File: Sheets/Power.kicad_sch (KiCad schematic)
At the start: 36 parts, among them J201 JST-XH 6P, Q201 FDV301N, Q202 FDV301N, Q203 SSF3365, SW201 SW, U201 LM2678SX-5.0, U202 BQ7720700DSSR, U203 LM2675M-12

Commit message: Rev 2.1 Add pcb and footprint changes
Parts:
- J201: footprint Connector_JST:JST_XH_B6B-XH-A_1x06_P2.50mm_Vertical -> Connector_JST:JST_XH_S6B-XH-A-1_1x06_P2.50mm_Horizontal
- Q203: footprint (none) -> Package_TO_SOT_SMD:SOT-23-3
- SW201, TH201: footprint Connector_JST:JST_ZH_B2B-ZR_1x02_P1.50mm_Vertical -> Connector_JST:JST_ZH_S2B-ZR-SM4A-TF_1x02-1MP_P1.50mm_Horizontal
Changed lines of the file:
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@@
 		(title "Cyclops (Team 30)")
 		(date "2025-11-28")
-		(rev "2.0")
+		(rev "2.1")
 		(company "Concordia University, Department of Electrical and Computer Engineering")
 	)
@@
 			)
 		)
-		(property "Footprint" "Connector_JST:JST_ZH_B2B-ZR_1x02_P1.50mm_Vertical"
+		(property "Footprint" "Connector_JST:JST_ZH_S2B-ZR-SM4A-TF_1x02-1MP_P1.50mm_Horizontal"
 			(at 107.95 46.99 0)
 			(effects
@@
 			)
 		)
-		(property "Footprint" "Connector_JST:JST_XH_B6B-XH-A_1x06_P2.50mm_Vertical"
+		(property "Footprint" "Connector_JST:JST_XH_S6B-XH-A-1_1x06_P2.50mm_Horizontal"
 			(at 55.88 73.66 0)
 			(effects
@@
 			)
 		)
-		(property "Footprint" ""
+		(property "Footprint" "Package_TO_SOT_SMD:SOT-23-3"
 			(at 182.88 22.86 0)
 			(effects
@@
 			)
 		)
-		(property "Footprint" "Connector_JST:JST_ZH_B2B-ZR_1x02_P1.50mm_Vertical"
+		(property "Footprint" "Connector_JST:JST_ZH_S2B-ZR-SM4A-TF_1x02-1MP_P1.50mm_Horizontal"
 			(at 195.58 50.8 0)
 			(effects

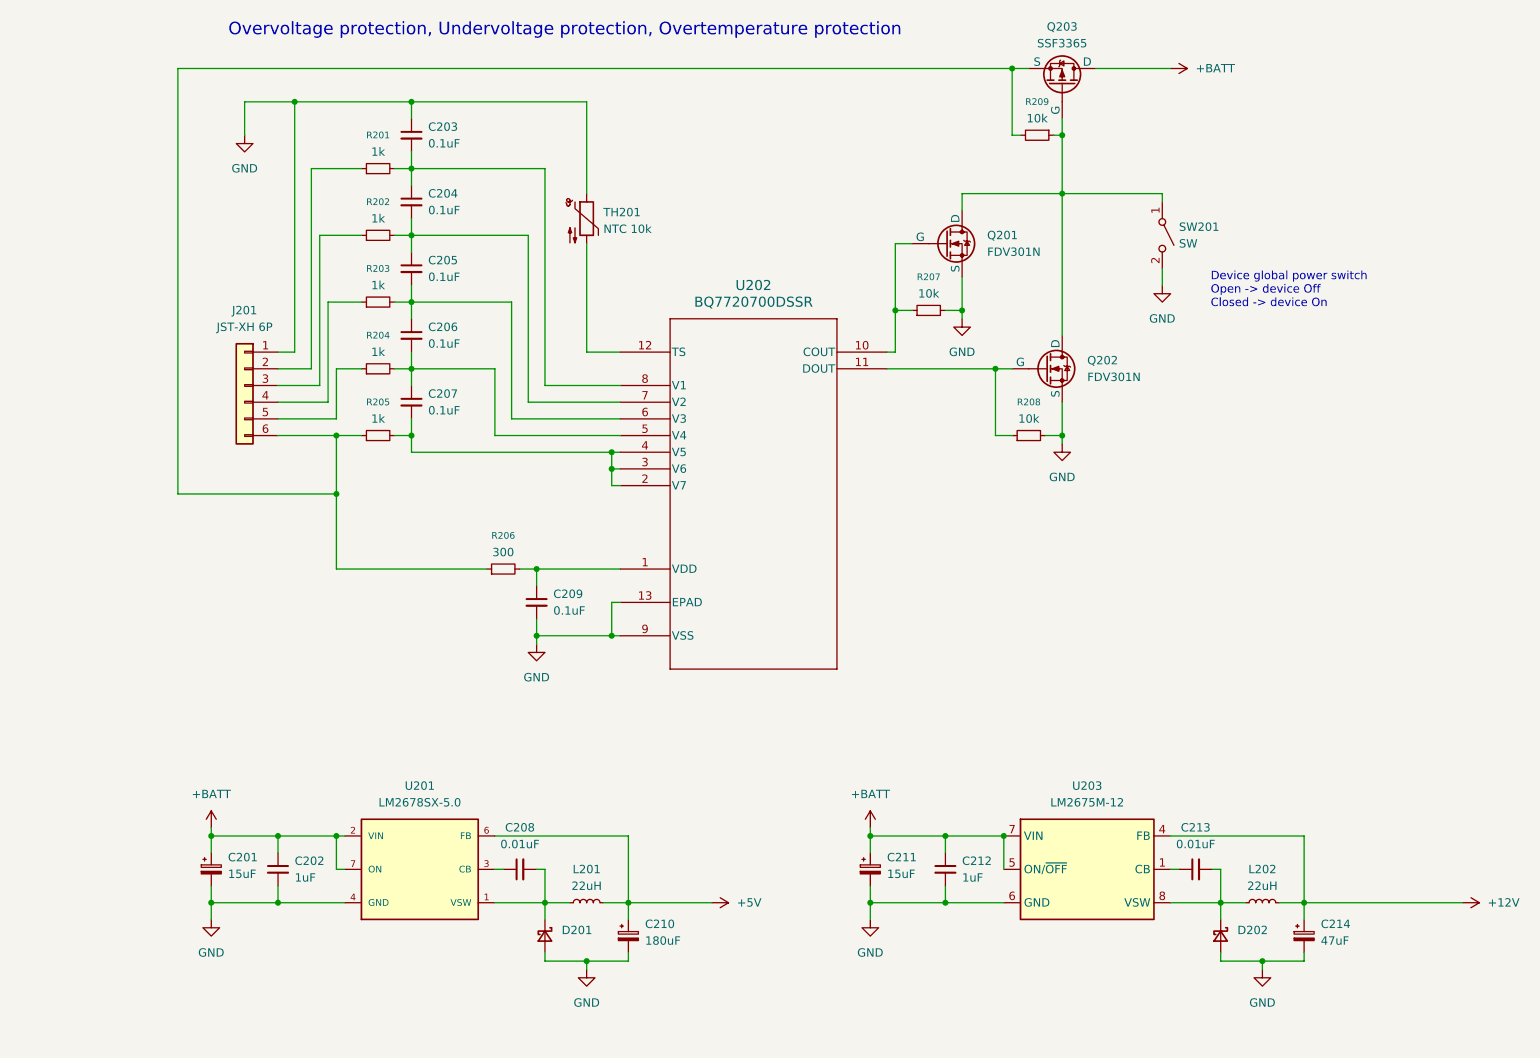
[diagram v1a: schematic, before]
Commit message: Rev 2.2 Added test point and status LED
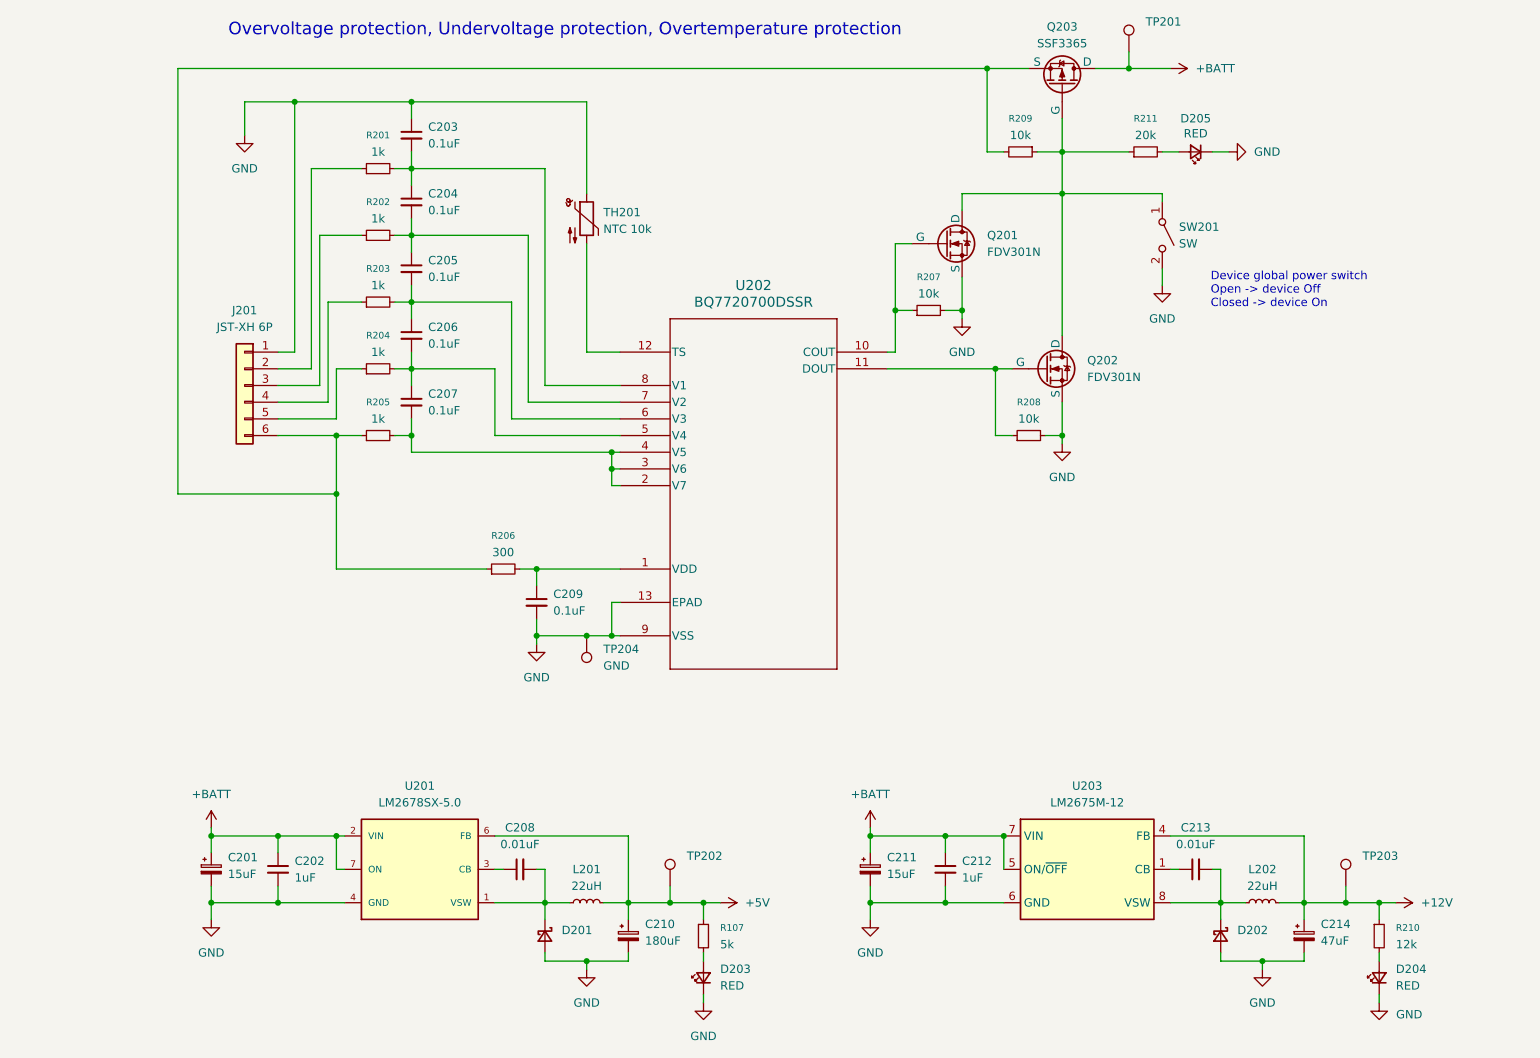
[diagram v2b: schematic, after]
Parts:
- added D203, D204, D205: RED, LED_SMD:LED_0603_1608Metric_Pad1.05x0.95mm_HandSolder, symbol Device:LED_Small
- added R107: 5k, Resistor_SMD:R_1206_3216Metric_Pad1.30x1.75mm_HandSolder, symbol Device:R_Small
- added R210: 12k, Resistor_SMD:R_1206_3216Metric_Pad1.30x1.75mm_HandSolder, symbol Device:R_Small
- added R211: 20k, Resistor_SMD:R_1206_3216Metric_Pad1.30x1.75mm_HandSolder, symbol Device:R_Small
- added TP201, TP202, TP203: ~, TestPoint:TestPoint_Pad_D2.5mm, symbol Connector:TestPoint
- added TP204: GND, TestPoint:TestPoint_Pad_D2.5mm, symbol Connector:TestPoint
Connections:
- net +12V: now also R210.1, TP203.1
- net +5V: now also R107.1, TP202.1
- net +BATT: now also TP201.1
- net GND: now also D203.1 (K), D204.1 (K), D205.1 (K), TP204.1
- net at Q201.1 (D), Q202.1 (D), Q203.2 (G)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: now also R211.1
- new net: D203.2 (A), R107.2
- new net: D205.2 (A), R211.2
- new net: D204.2 (A), R210.2
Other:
- moved on the sheet: R209

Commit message: Rev 2.3 New battery protection IC and various other changes
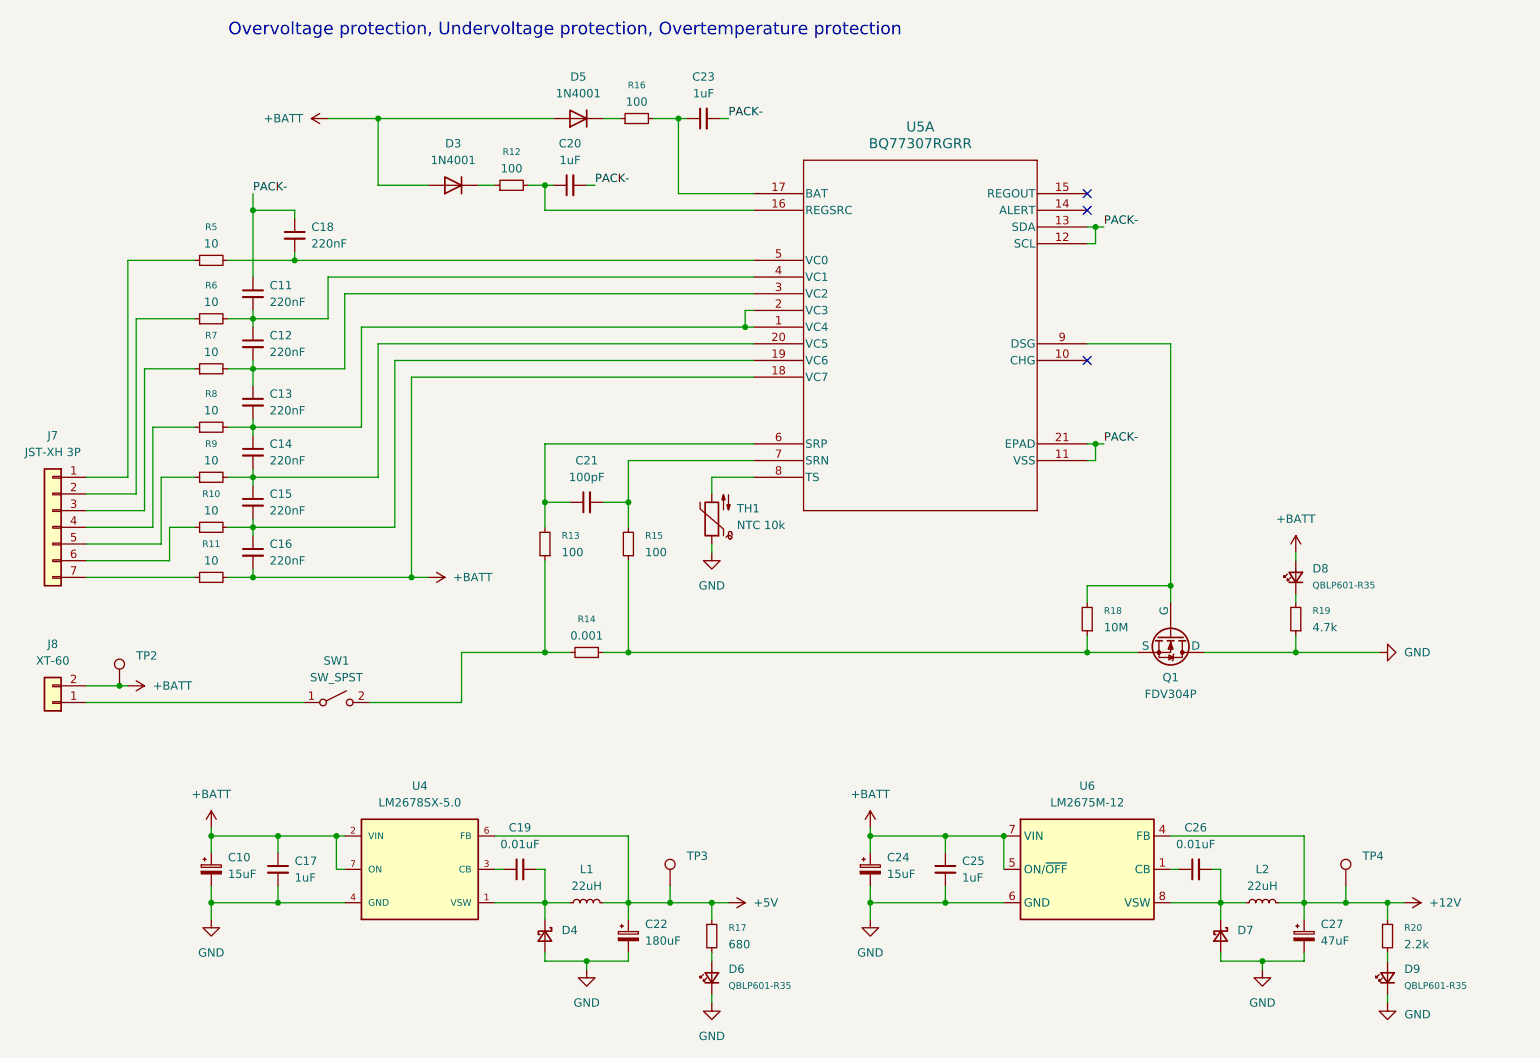
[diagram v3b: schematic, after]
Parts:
- removed C203, C204, C205, C206, C207, C209: 0.1uF, Capacitor_SMD:C_1206_3216Metric_Pad1.33x1.80mm_HandSolder, symbol Device:C_Small
- removed D205: RED, LED_SMD:LED_0603_1608Metric_Pad1.05x0.95mm_HandSolder, symbol Device:LED_Small
- removed J201: JST-XH 6P, Connector_JST:JST_XH_S6B-XH-A-1_1x06_P2.50mm_Horizontal, symbol Connector_Generic:Conn_01x06
- removed Q201, Q202: FDV301N, Package_TO_SOT_SMD:SOT-23-3, symbol Simulation_SPICE:NMOS
- removed Q203: SSF3365, Package_TO_SOT_SMD:SOT-23-3, symbol Simulation_SPICE:PMOS
- removed R201, R202, R203, R204, R205: 1k, Resistor_SMD:R_1206_3216Metric_Pad1.30x1.75mm_HandSolder, symbol Device:R_Small
- removed R206: 300, Resistor_SMD:R_1206_3216Metric_Pad1.30x1.75mm_HandSolder, symbol Device:R_Small
- removed R207, R208, R209: 10k, Resistor_SMD:R_1206_3216Metric_Pad1.30x1.75mm_HandSolder, symbol Device:R_Small
- removed R211: 20k, Resistor_SMD:R_1206_3216Metric_Pad1.30x1.75mm_HandSolder, symbol Device:R_Small
- removed SW201: SW, Connector_JST:JST_ZH_S2B-ZR-SM4A-TF_1x02-1MP_P1.50mm_Horizontal, symbol Switch:SW_SPST
- removed TP201: ~, TestPoint:TestPoint_Pad_D2.5mm, symbol Connector:TestPoint
- removed TP204: GND, TestPoint:TestPoint_Pad_D2.5mm, symbol Connector:TestPoint
- removed U202: BQ7720700DSSR, Package_SON:WSON-12-1EP_3x2mm_P0.5mm_EP1x2.65, symbol BQ7720700DSSR:BQ7720700DSSR
- added C11, C12, C13, C14, C15, C16, C18: 220nF, Capacitor_SMD:C_1206_3216Metric_Pad1.33x1.80mm_HandSolder, symbol Device:C_Small
- added C20, C23: 1uF, Capacitor_SMD:C_1206_3216Metric_Pad1.33x1.80mm_HandSolder, symbol Device:C_Small
- added C21: 100pF, Capacitor_SMD:C_1206_3216Metric_Pad1.33x1.80mm_HandSolder, symbol Device:C_Small
- added D3, D5: 1N4001, Diode_THT:D_DO-41_SOD81_P10.16mm_Horizontal, symbol Diode:1N4001
- added D8: QBLP601-R35, LED_SMD:LED_0603_1608Metric_Pad1.05x0.95mm_HandSolder, symbol Device:LED_Small
- added J7: JST-XH 3P, Connector_JST:JST_XH_S7B-XH-A_1x07_P2.50mm_Horizontal, symbol Connector_Generic:Conn_01x07
- added J8: XT-60, Connector_AMASS:AMASS_XT60PW-F_1x02_P7.20mm_Horizontal, symbol Connector_Generic:Conn_01x02
- added Q1: FDV304P, Package_TO_SOT_SMD:SOT-23-3, symbol Simulation_SPICE:NMOS
- added R10, R11, R5, R6, R7, R8, R9: 10, Resistor_SMD:R_1206_3216Metric_Pad1.30x1.75mm_HandSolder, symbol Device:R_Small
- added R12, R13, R15, R16: 100, Resistor_SMD:R_1206_3216Metric_Pad1.30x1.75mm_HandSolder, symbol Device:R_Small
- added R14: 0.001, Resistor_SMD:R_1206_3216Metric_Pad1.30x1.75mm_HandSolder, symbol Device:R_Small
- added R18: 10M, Resistor_SMD:R_1206_3216Metric_Pad1.30x1.75mm_HandSolder, symbol Device:R_Small
- added R19: 4.7k, Resistor_SMD:R_1206_3216Metric_Pad1.30x1.75mm_HandSolder, symbol Device:R_Small
- added SW1: SW_SPST, TestPoint:TestPoint_Bridge_Pitch3.81mm_Drill1.3mm, symbol Switch:SW_SPST
- added TP2: ~, TestPoint:TestPoint_Pad_D2.5mm, symbol Connector:TestPoint
- added U5: BQ77307RGRR, Package_DFN_QFN:Texas_RGP0020D_VQFN-20-1EP_4x4mm_P0.5mm_EP2.7x2.7mm, symbol ul_BQ77307RGRR:BQ77307RGRR
- D6: renamed from D203; value RED -> QBLP601-R35
- D9: renamed from D204; value RED -> QBLP601-R35
- R17: renamed from R107; value 5k -> 680
- R20: renamed from R210; value 12k -> 2.2k
- renumbered C201 to C10, C202 to C17, C208 to C19, C210 to C22, C211 to C24, C212 to C25, C213 to C26, C214 to C27, D201 to D4, D202 to D7, L201 to L1, L202 to L2, TH201 to TH1, TP202 to TP3, TP203 to TP4, U201 to U4, U203 to U6
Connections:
- net +BATT: now also C16.2, D3.2 (A), D5.2 (A), D8.2 (A), J8.2 (Pin_2), R11.2, TP2.1, U5.18 (VC7)
- net GND: now also Q1.1 (D), R19.1
- net at TH1.2: now also U5.8 (TS)
- new net: Q1.3 (S), R14.1, R15.1, R18.1
- new net: R13.1, R14.2, SW1.2 (B)
- new net: C13.2, C14.1, R8.2, U5.1 (VC4), U5.2 (VC3)
- new net: C14.2, C15.1, R9.2, U5.20 (VC5)
- new net: C11.2, C12.1, R6.2, U5.4 (VC1)
- new net: C23.1, R16.2, U5.17 (BAT)
- new net: C21.2, R15.2, U5.7 (SRN)
- new net: J7.4 (Pin_4), R8.1
- new net: J8.1 (Pin_1), SW1.1 (A)
- new net: C12.2, C13.1, R7.2, U5.3 (VC2)
- new net: J7.1 (Pin_1), R5.1
- new net: J7.2 (Pin_2), R6.1
- new net: J7.3 (Pin_3), R7.1
- new net: J7.5 (Pin_5), R9.1
- new net: J7.6 (Pin_6), R10.1
- new net: J7.7 (Pin_7), R11.1
- new net: D3.1 (K), R12.1
- new net: C21.1, R13.2, U5.6 (SRP)
- new net: C15.2, C16.1, R10.2, U5.19 (VC6)
- new net: C20.1, R12.2, U5.16 (REGSRC)
- new net: C18.2, R5.2, U5.5 (VC0)
- new net: Q1.2 (G), R18.2, U5.9 (DSG)
- new net: D5.1 (K), R16.1
- new net: D8.1 (K), R19.2
- new net PACK-: C11.1, C18.1, C20.2, C23.2, U5.11 (VSS), U5.12 (SCL), U5.13 (SDA), U5.21 (EPAD)
- no-connect marks 0 -> 3
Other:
- note removed: "Device global power switch Open -> device Off Closed -> device On"
- moved on the sheet: D6, D9, R17, R20, TH1

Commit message: Rev 2.4
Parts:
- removed C10, C24: 15uF, Capacitor_THT:CP_Radial_D5.0mm_P2.50mm, symbol Device:C_Polarized_Small
- removed Q1: FDV304P, Package_TO_SOT_SMD:SOT-23-3, symbol Simulation_SPICE:NMOS
- added C11, C25: 47uF, Capacitor_SMD:C_0805_2012Metric_Pad1.18x1.45mm_HandSolder, symbol Device:C_Small
- added J9: 01x03_Pin, Connector_PinHeader_2.54mm:PinHeader_1x03_P2.54mm_Horizontal, symbol Connector:Conn_01x03_Pin
- added Q2: FDV304P, Package_TO_SOT_SMD:SOT-23-3, symbol Simulation_SPICE:PMOS
- C12: renamed from C11; footprint Capacitor_SMD:C_1206_3216Metric_Pad1.33x1.80mm_HandSolder -> Capacitor_SMD:C_0805_2012Metric_Pad1.18x1.45mm_HandSolder
- C13: renamed from C12; footprint Capacitor_SMD:C_1206_3216Metric_Pad1.33x1.80mm_HandSolder -> Capacitor_SMD:C_0805_2012Metric_Pad1.18x1.45mm_HandSolder
- C14: renamed from C13; footprint Capacitor_SMD:C_1206_3216Metric_Pad1.33x1.80mm_HandSolder -> Capacitor_SMD:C_0805_2012Metric_Pad1.18x1.45mm_HandSolder
- C15: renamed from C14; footprint Capacitor_SMD:C_1206_3216Metric_Pad1.33x1.80mm_HandSolder -> Capacitor_SMD:C_0805_2012Metric_Pad1.18x1.45mm_HandSolder
- C16: renamed from C15; footprint Capacitor_SMD:C_1206_3216Metric_Pad1.33x1.80mm_HandSolder -> Capacitor_SMD:C_0805_2012Metric_Pad1.18x1.45mm_HandSolder
- C17: renamed from C16; footprint Capacitor_SMD:C_1206_3216Metric_Pad1.33x1.80mm_HandSolder -> Capacitor_SMD:C_0805_2012Metric_Pad1.18x1.45mm_HandSolder
- C18: renamed from C17; footprint Capacitor_SMD:C_1206_3216Metric_Pad1.33x1.80mm_HandSolder -> Capacitor_SMD:C_0805_2012Metric_Pad1.18x1.45mm_HandSolder
- C19: renamed from C18; footprint Capacitor_SMD:C_1206_3216Metric_Pad1.33x1.80mm_HandSolder -> Capacitor_SMD:C_0805_2012Metric_Pad1.18x1.45mm_HandSolder
- C20: renamed from C19; footprint Capacitor_SMD:C_1206_3216Metric_Pad1.33x1.80mm_HandSolder -> Capacitor_SMD:C_0805_2012Metric_Pad1.18x1.45mm_HandSolder
- C21: renamed from C20; footprint Capacitor_SMD:C_1206_3216Metric_Pad1.33x1.80mm_HandSolder -> Capacitor_SMD:C_0805_2012Metric_Pad1.18x1.45mm_HandSolder
- C22: renamed from C21; footprint Capacitor_SMD:C_1206_3216Metric_Pad1.33x1.80mm_HandSolder -> Capacitor_SMD:C_0805_2012Metric_Pad1.18x1.45mm_HandSolder
- C24: renamed from C23; footprint Capacitor_SMD:C_1206_3216Metric_Pad1.33x1.80mm_HandSolder -> Capacitor_SMD:C_0805_2012Metric_Pad1.18x1.45mm_HandSolder
- C26: renamed from C25; footprint Capacitor_SMD:C_1206_3216Metric_Pad1.33x1.80mm_HandSolder -> Capacitor_SMD:C_0805_2012Metric_Pad1.18x1.45mm_HandSolder
- C27: renamed from C26; footprint Capacitor_SMD:C_1206_3216Metric_Pad1.33x1.80mm_HandSolder -> Capacitor_SMD:C_0805_2012Metric_Pad1.18x1.45mm_HandSolder
- C28: renamed from C27; footprint Capacitor_SMD:C_1206_3216Metric_Pad1.33x1.80mm_HandSolder -> Capacitor_SMD:C_0805_2012Metric_Pad1.18x1.45mm_HandSolder
- D3, D5: value 1N4001 -> 1N4148W; footprint Diode_THT:D_DO-41_SOD81_P10.16mm_Horizontal -> Diode_SMD:D_SOD-123
- D4: value ~ -> SK35; footprint Diode_THT:D_DO-41_SOD81_P10.16mm_Horizontal -> Diode_SMD:D_SMB-SMC_Universal_Handsoldering
- D7: value ~ -> SK15; footprint Diode_THT:D_DO-41_SOD81_P10.16mm_Horizontal -> Diode_SMD:D_SMA-SMB_Universal_Handsoldering
- J7: value JST-XH 3P -> JST-XH 7P
- J8: value XT-60 -> XT60
- R10: renamed from R8; footprint Resistor_SMD:R_1206_3216Metric_Pad1.30x1.75mm_HandSolder -> Resistor_SMD:R_0805_2012Metric_Pad1.20x1.40mm_HandSolder
- R11: renamed from R9; footprint Resistor_SMD:R_1206_3216Metric_Pad1.30x1.75mm_HandSolder -> Resistor_SMD:R_0805_2012Metric_Pad1.20x1.40mm_HandSolder
- R12: renamed from R10; footprint Resistor_SMD:R_1206_3216Metric_Pad1.30x1.75mm_HandSolder -> Resistor_SMD:R_0805_2012Metric_Pad1.20x1.40mm_HandSolder
- R13: renamed from R11; footprint Resistor_SMD:R_1206_3216Metric_Pad1.30x1.75mm_HandSolder -> Resistor_SMD:R_0805_2012Metric_Pad1.20x1.40mm_HandSolder
- R14: renamed from R12; value 100 -> 10; footprint Resistor_SMD:R_1206_3216Metric_Pad1.30x1.75mm_HandSolder -> Resistor_SMD:R_0805_2012Metric_Pad1.20x1.40mm_HandSolder
- R15: renamed from R13; footprint Resistor_SMD:R_1206_3216Metric_Pad1.30x1.75mm_HandSolder -> Resistor_SMD:R_0805_2012Metric_Pad1.20x1.40mm_HandSolder
- R17: renamed from R15; footprint Resistor_SMD:R_1206_3216Metric_Pad1.30x1.75mm_HandSolder -> Resistor_SMD:R_0805_2012Metric_Pad1.20x1.40mm_HandSolder
- R18: renamed from R16; footprint Resistor_SMD:R_1206_3216Metric_Pad1.30x1.75mm_HandSolder -> Resistor_SMD:R_0805_2012Metric_Pad1.20x1.40mm_HandSolder
- R19: renamed from R17; footprint Resistor_SMD:R_1206_3216Metric_Pad1.30x1.75mm_HandSolder -> Resistor_SMD:R_0805_2012Metric_Pad1.20x1.40mm_HandSolder
- R20: renamed from R18; footprint Resistor_SMD:R_1206_3216Metric_Pad1.30x1.75mm_HandSolder -> Resistor_SMD:R_0805_2012Metric_Pad1.20x1.40mm_HandSolder
- R21: renamed from R19; footprint Resistor_SMD:R_1206_3216Metric_Pad1.30x1.75mm_HandSolder -> Resistor_SMD:R_0805_2012Metric_Pad1.20x1.40mm_HandSolder
- R22: renamed from R20; footprint Resistor_SMD:R_1206_3216Metric_Pad1.30x1.75mm_HandSolder -> Resistor_SMD:R_0805_2012Metric_Pad1.20x1.40mm_HandSolder
- R7: renamed from R5; footprint Resistor_SMD:R_1206_3216Metric_Pad1.30x1.75mm_HandSolder -> Resistor_SMD:R_0805_2012Metric_Pad1.20x1.40mm_HandSolder
- R8: renamed from R6; footprint Resistor_SMD:R_1206_3216Metric_Pad1.30x1.75mm_HandSolder -> Resistor_SMD:R_0805_2012Metric_Pad1.20x1.40mm_HandSolder
- R9: renamed from R7; footprint Resistor_SMD:R_1206_3216Metric_Pad1.30x1.75mm_HandSolder -> Resistor_SMD:R_0805_2012Metric_Pad1.20x1.40mm_HandSolder
- SW1: value SW_SPST -> RA11131100; footprint TestPoint:TestPoint_Bridge_Pitch3.81mm_Drill1.3mm -> TestPoint:TestPoint_2Pads_Pitch5.08mm_Drill1.3mm
- TP2, TP3, TP4: footprint TestPoint:TestPoint_Pad_D2.5mm -> TestPoint:TestPoint_Pad_D1.5mm
- U8: renamed from U6; value LM2675M-12 -> LM2675MX-12
- renumbered C22 to C23, R14 to R16, U4 to U6, U5 to U7
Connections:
- net +BATT: now also C11.1, C25.1; no longer U8.5 (ON/~{OFF})
- net GND: now also C11.2, C25.2, Q2.1 (D); no longer TH1.1
- net PACK-: now also R15.1, R16.2, SW1.2 (B), TH1.1, J9.1 (Pin_1); no longer U7.12 (SCL), U7.13 (SDA)
- net at R16.1, R17.1, R20.1: now also Q2.3 (S)
- net at J7.1 (Pin_1): now also R13.1; no longer R7.1
- net at J7.2 (Pin_2): now also R12.1; no longer R8.1
- net at J7.3 (Pin_3): now also R11.1; no longer R9.1
- net at J7.5 (Pin_5): now also R9.1; no longer R11.1
- net at J7.6 (Pin_6): now also R8.1; no longer R12.1
- net at J7.7 (Pin_7): now also R7.1; no longer R13.1
- net at R20.2, U7.9 (DSG): now also Q2.2 (G)
- new net SCL: J9.2 (Pin_2), U7.12 (SCL)
- new net SDA: J9.3 (Pin_3), U7.13 (SDA)
- no-connect marks 3 -> 4
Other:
- note added: "Undervoltage protection, Short circuit, and Overtemperature protection"
- note removed: "Overvoltage protection, Undervoltage protection, Overtemperature protection"
- moved on the sheet: C18, C20, C23, C28, D4, D6, D7, J7, L1, R19, TP3, U6
